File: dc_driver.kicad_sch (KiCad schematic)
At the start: 30 parts, among them U2 L298N, U3 L298N, U4 L298N

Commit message: schematic finished
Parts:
- removed D1, D10, D11, D12, D17, D18, D19, D2, D20, D21, D22, D23, D24, D3, D4, D9: SS34-DO214AB-HT, Diode_SMD:D_SMC, symbol Device:D_Small
- added D13, D14, D15, D16, D32, D33, D34, D35, D36, D37, D38, D39, D5, D6, D7, D8: 1N4007, Diode_SMD:D_SOD-123, symbol Device:D_Small
- C13: footprint (none) -> Capacitor_SMD:CP_Elec_8x10.5
- D1: renamed from D5; value SS34-DO214AB-HT -> 1N4007; footprint Diode_SMD:D_SMC -> Diode_SMD:D_SOD-123
- D10: renamed from D14; value SS34-DO214AB-HT -> 1N4007; footprint Diode_SMD:D_SMC -> Diode_SMD:D_SOD-123
- D11: renamed from D15; value SS34-DO214AB-HT -> 1N4007; footprint Diode_SMD:D_SMC -> Diode_SMD:D_SOD-123
- D12: renamed from D16; value SS34-DO214AB-HT -> 1N4007; footprint Diode_SMD:D_SMC -> Diode_SMD:D_SOD-123
- D2: renamed from D6; value SS34-DO214AB-HT -> 1N4007; footprint Diode_SMD:D_SMC -> Diode_SMD:D_SOD-123
- D3: renamed from D7; value SS34-DO214AB-HT -> 1N4007; footprint Diode_SMD:D_SMC -> Diode_SMD:D_SOD-123
- D4: renamed from D8; value SS34-DO214AB-HT -> 1N4007; footprint Diode_SMD:D_SMC -> Diode_SMD:D_SOD-123
- D9: renamed from D13; value SS34-DO214AB-HT -> 1N4007; footprint Diode_SMD:D_SMC -> Diode_SMD:D_SOD-123
- renumbered C12 to C11, C11 to C12, U3 to U2, U2 to U3
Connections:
- net DC3_1: now also D32.2 (A), D36.1 (K)
- net DC3_2: now also D33.2 (A), D37.1 (K)
- net DC4_1: now also D34.2 (A), D38.1 (K)
- net DC5_1: now also D13.1 (K), D5.2 (A)
- net DC5_2: now also D14.1 (K), D35.2 (A), D39.1 (K), D6.2 (A)
- net DC6_1: now also D15.1 (K), D7.2 (A)
- net DC6_2: now also D16.1 (K), D8.2 (A)
- net GND: now also D13.2 (A), D14.2 (A), D15.2 (A), D16.2 (A), D36.2 (A), D37.2 (A), D38.2 (A), D39.2 (A)
- net VIN: now reaches C11.1, D1.1 (K), D2.1 (K), D3.1 (K), D4.1 (K), U2.4 (Vs)
- net VIN: now also C12.1, C13.1, U3.4 (Vs), U4.4 (Vs), D32.1 (K), D33.1 (K), D34.1 (K), D35.1 (K), D5.1 (K), D6.1 (K), D7.1 (K), D8.1 (K)

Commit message: Power Routing
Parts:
- added R10, R17, R18, R58, R59, R60: 12k, Resistor_SMD:R_0805_2012Metric, symbol Device:R_Small
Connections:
- net DCEn1: now also R10.2; no longer U2.6 (EnA)
- net DCEn2: now also R17.2; no longer U2.11 (EnB)
- net DCEn3: now also R18.2; no longer U3.6 (EnA)
- net DCEn4: now also R58.2; no longer U3.11 (EnB)
- net DCEn5: now also R59.2; no longer U4.6 (EnA)
- net DCEn6: now also R60.2; no longer U4.11 (EnB)
- new net: R17.1, U2.11 (EnB)
- new net: R10.1, U2.6 (EnA)
- new net: R58.1, U3.11 (EnB)
- new net: R18.1, U3.6 (EnA)
- new net: R59.1, U4.6 (EnA)
- new net: R60.1, U4.11 (EnB)

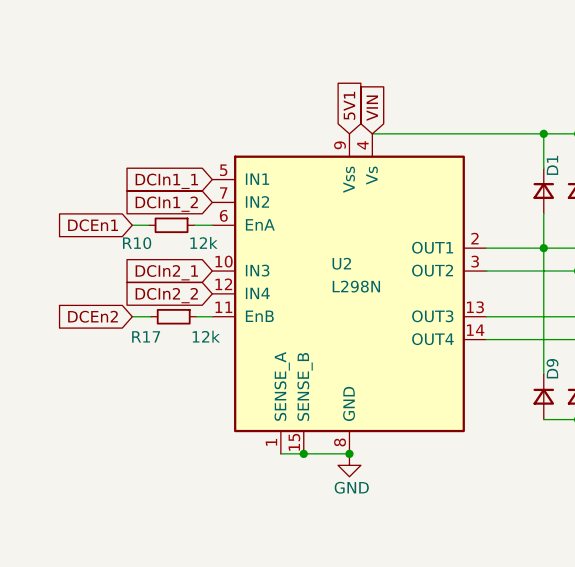
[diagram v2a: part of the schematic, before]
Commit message: Reapply "placing completed."
This reverts commit 83f85ef5575867dc78eeeae3514badb4960c2205.
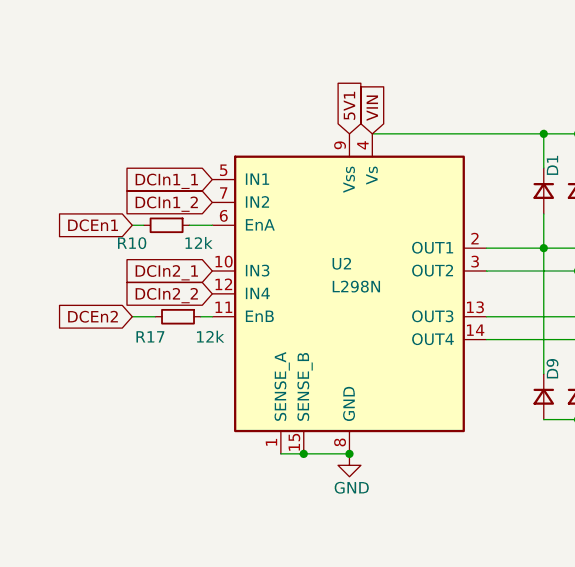
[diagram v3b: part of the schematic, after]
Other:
- moved on the sheet: R10
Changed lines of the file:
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@@
 	(wire
 		(pts
-			(xy 31.0327 41.91) (xy 33.02 41.91)
+			(xy 30.48 41.91) (xy 33.02 41.91)
 		)
 		(stroke
@@
 	(wire
 		(pts
-			(xy 31.2709 52.07) (xy 33.02 52.07)
+			(xy 31.75 52.07) (xy 33.02 52.07)
 		)
 		(stroke
@@
 	(wire
 		(pts
-			(xy 24.13 52.07) (xy 26.1909 52.07)
+			(xy 24.13 52.07) (xy 26.67 52.07)
 		)
 		(stroke
@@
 	(wire
 		(pts
-			(xy 24.13 41.91) (xy 25.9527 41.91)
+			(xy 24.13 41.91) (xy 25.4 41.91)
 		)
 		(stroke
@@
 	(symbol
 		(lib_id "Device:R_Small")
-		(at 28.7309 52.07 270)
+		(at 29.21 52.07 270)
 		(unit 1)
 		(exclude_from_sim no)
@@
 		(dnp no)
 		(property "Reference" "R17"
-			(at 25.654 54.356 90)
+			(at 26.1331 54.356 90)
 			(effects
 				(font
@@
 		)
 		(property "Value" "12k"
-			(at 32.258 54.356 90)
+			(at 32.7371 54.356 90)
 			(effects
 				(font
@@
 		)
 		(property "Footprint" "Resistor_SMD:R_0805_2012Metric"
-			(at 28.7309 52.07 0)
+			(at 29.21 52.07 0)
 			(effects
 				(font
@@
 		)
 		(property "Datasheet" "~"
-			(at 28.7309 52.07 0)
+			(at 29.21 52.07 0)
 			(effects
 				(font
@@
 		)
 		(property "Description" "Resistor, small symbol"
-			(at 28.7309 52.07 0)
+			(at 29.21 52.07 0)
 			(effects
 				(font
@@
 	(symbol
 		(lib_id "Device:R_Small")
-		(at 28.4927 41.91 270)
+		(at 27.94 41.91 270)
 		(unit 1)
 		(exclude_from_sim no)
@@
 		(dnp no)
 		(property "Reference" "R10"
-			(at 24.638 43.942 90)
+			(at 24.0853 43.942 90)
 			(effects
 				(font
@@
 		)
 		(property "Value" "12k"
-			(at 32.004 43.942 90)
+			(at 31.4513 43.942 90)
 			(effects
 				(font
@@
 		)
 		(property "Footprint" "Resistor_SMD:R_0805_2012Metric"
-			(at 28.4927 41.91 0)
+			(at 27.94 41.91 0)
 			(effects
 				(font
@@
 		)
 		(property "Datasheet" "~"
-			(at 28.4927 41.91 0)
+			(at 27.94 41.91 0)
 			(effects
 				(font
@@
 		)
 		(property "Description" "Resistor, small symbol"
-			(at 28.4927 41.91 0)
+			(at 27.94 41.91 0)
 			(effects
 				(font

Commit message: esp32 silindi, yerleştirmeler yapıldı
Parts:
- removed C11, C12, C13: 220uF 35V, Capacitor_SMD:CP_Elec_8x10.5, symbol Device:C_Polarized_Small
- removed D1, D10, D11, D12, D13, D14, D15, D16, D2, D3, D32, D33, D34, D35, D36, D37, D38, D39, D4, D5, D6, D7, D8, D9: 1N4007, Diode_SMD:D_SOD-123, symbol Device:D_Small
- removed R10, R17, R18, R58, R59, R60: 12k, Resistor_SMD:R_0805_2012Metric, symbol Device:R_Small
- removed U2, U3, U4: L298N, Package_TO_SOT_THT:TO-220-15_P2.54x2.54mm_StaggerOdd_Lead4.58mm_Vertical, symbol Driver_Motor:L298N
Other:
- added sheet L298N (L298N.kicad_sch)
- added sheet L298N1 (L298N.kicad_sch)
- added sheet L298N2 (L298N.kicad_sch)
